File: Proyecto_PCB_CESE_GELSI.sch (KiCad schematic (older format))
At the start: 20 parts, among them IC1 SC2272L4, IC2 ASM1117-33, IC3 SN74LVC1G125DCKR, IC4 H5V3G

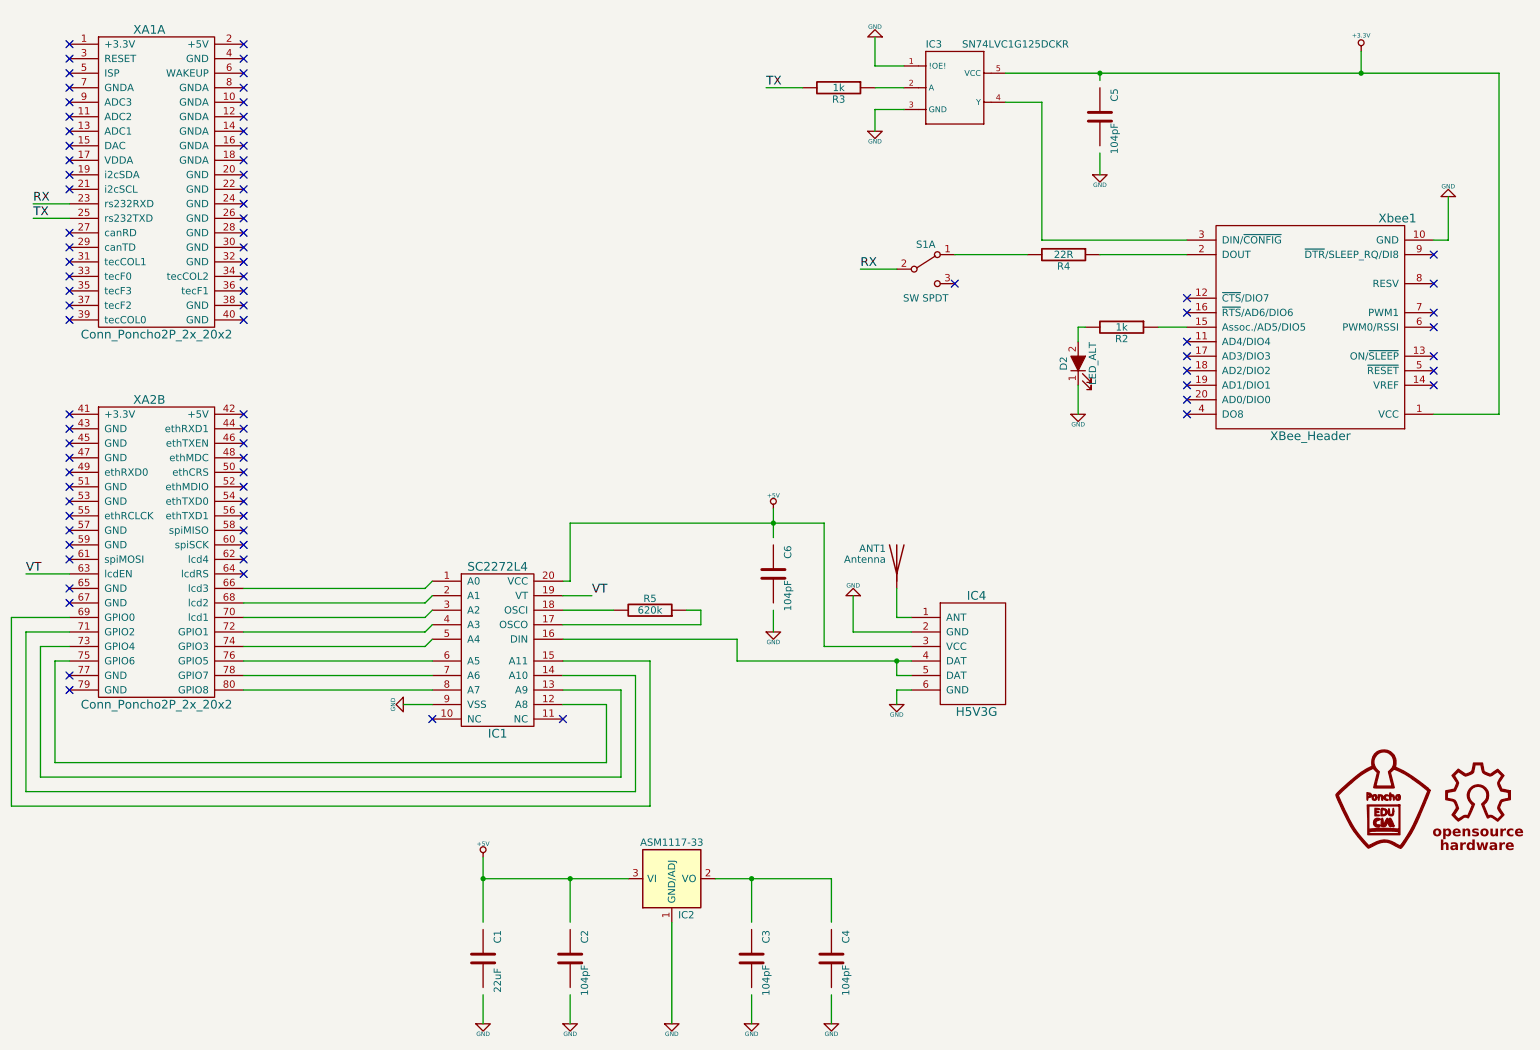
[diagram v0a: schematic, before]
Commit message: Avance hacia cierre de esquemático y comienzo de pcb
Falta sólo realizar comentarios con etiquetas en el esquemático, de los subsistemas. Y por otro lado ya se comenzó con el pcb, se avanzó para poder preguntar en clases dudas respecto al tema de ruteado.
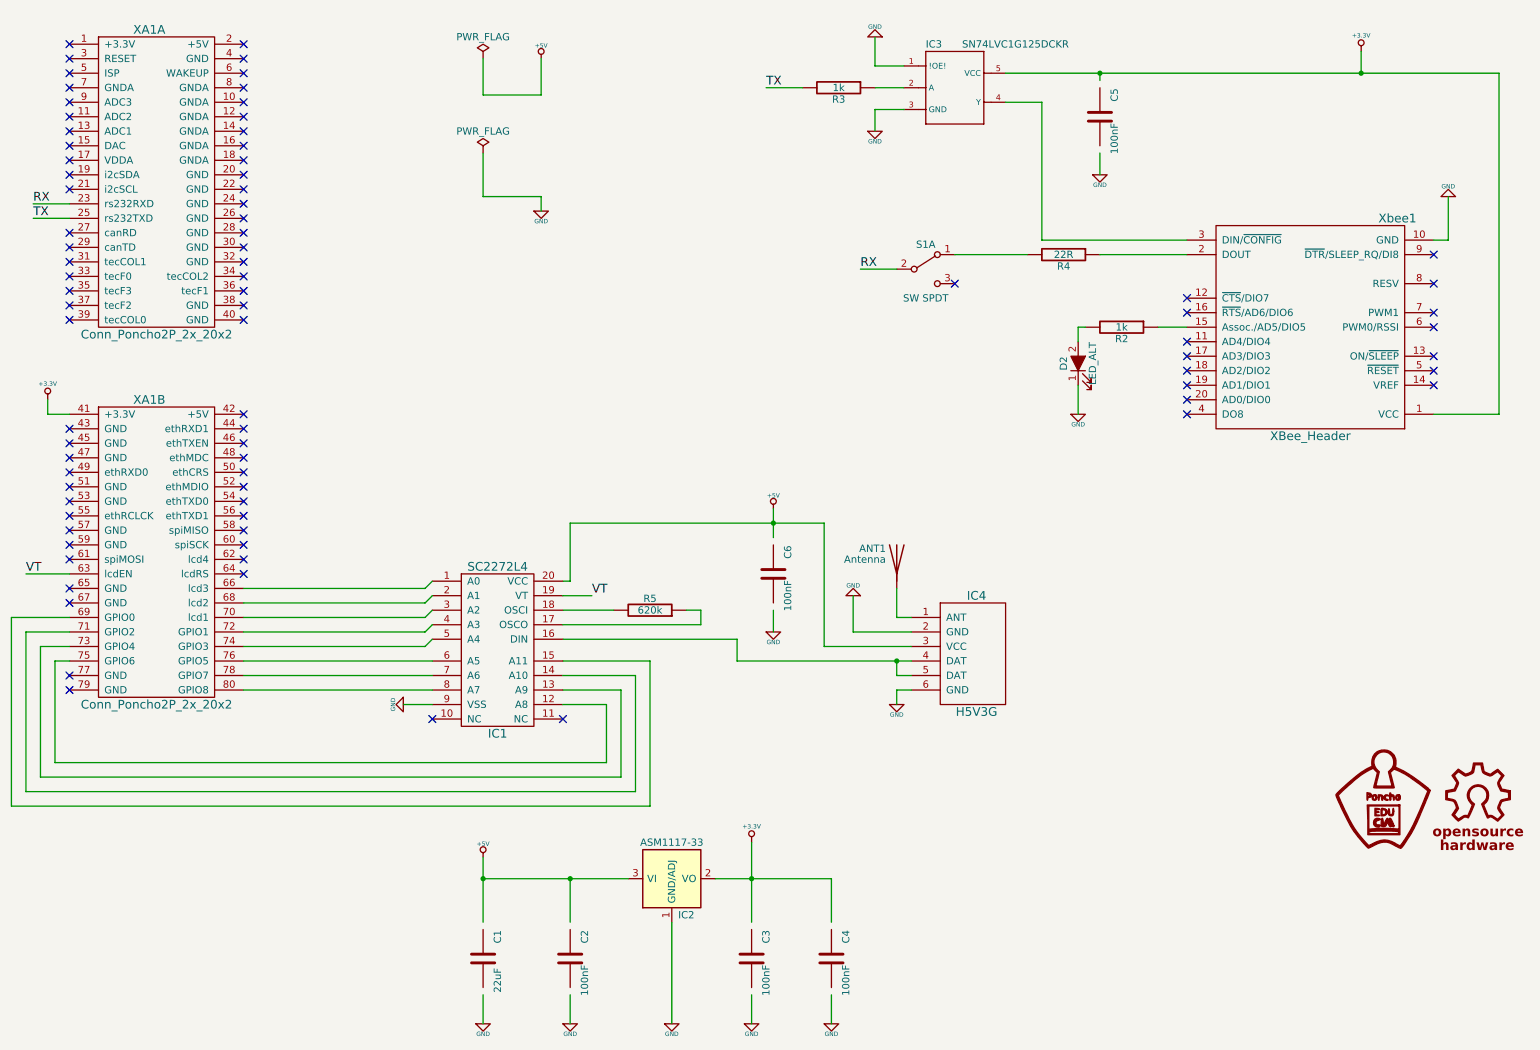
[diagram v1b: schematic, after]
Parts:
- ANT1: footprint (none) -> projectHuellas:antena
- C1: footprint (none) -> projectHuellas:C_0603_HandSoldering
- C2, C3, C4, C5, C6: value 104pF -> 100nF; footprint (none) -> projectHuellas:C_0603_HandSoldering
- D2: footprint (none) -> projectHuellas:D_0805
- IC1: footprint (none) -> projectHuellas:SSOP-20_5.3x7.2mm_Pitch0.65mm
- IC2: footprint TO_SOT_Packages_SMD:SOT-223 -> projectHuellas:SOT-223
- IC3: footprint SC-70-5 -> projectHuellas:SC-70-5
- IC4: footprint (none) -> projectHuellas:H5V3G
- R2, R3, R4, R5: footprint (none) -> projectHuellas:R_1206_HandSoldering
- S1: footprint (none) -> projectHuellas:SW_SPDT
- XA1: renamed from XA2; footprint (none) -> projectHuellas:Conn_Poncho_Completo
- XA1: footprint (none) -> projectHuellas:Conn_Poncho_Completo
- Xbee1: footprint (none) -> projectHuellas:XBEE-HEADER
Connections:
- wire segments 95 -> 103
- no-connect marks 83 -> 82

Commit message: Update en el proyecto
Se consolidaron datos en la mayoría de los componentes, como fabricante, parte dentro del fabricante, digikey, y descripción
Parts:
- C1: Desc (none) -> CAP CER 22UF 6.3V X5R 0603; Digikey# (none) -> 490-7611-1-ND; Manf (none) -> Murata Electronics North America; Manf# (none) -> GRM188R60J226MEA0D; Price (none) -> 0.24
- C2, C3, C4, C5, C6: Desc (none) -> CAP CER 0.1UF 6.3V X5R 0201; Digikey# (none) -> 478-5266-1-ND; Manf (none) -> AVX Corporation; Manf# (none) -> 02016D104KAT2A; Price (none) -> 0.10
- D2: Desc (none) -> LED GREEN DIFFUSED 0805 SMD; Digikey# (none) -> 475-1410-1-ND; Manf (none) -> OSRAM Opto Semiconductors Inc.; Manf# (none) -> LG R971-KN-1; Price (none) -> 0.25
- IC2: Desc (none) -> IC REG LDO 5V 1A SOT223; Digikey# (none) -> NCP1117ST50T3GOSCT-ND; Manf (none) -> ON Semiconductor; Manf# (none) -> NCP1117ST50T3G; Price (none) -> 0.50
- IC3: Desc (none) -> Buffer, Non-Inverting Element 1 Bit per Element Push-Pull O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; Description Buffer/Line%20Driver%201-CH%20Non-Inverting%203-ST%20CMOS%2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 -> (none); Digikey# (none) -> 296-11604-1-ND; Manf (none) -> Texas Instruments; Manf# (none) -> SN74LVC1G125DCKR; Price 0.14 USD -> 0.36 USD
- R2, R3: Desc (none) -> RES SMD 1K OHM 1% 1/4W 1206; Digikey# (none) -> 311-1.00KFRCT-ND; Manf (none) -> Yageo; Manf# (none) -> RC1206FR-071KL; Price (none) -> 0.10
- R4: Desc (none) -> RES SMD 22 OHM 5% 1/4W 1206; Digikey# (none) -> 311-22ERCT-ND; Manf (none) -> Yageo; Manf# (none) -> RC1206JR-0722RL; Price (none) -> 0.10
- R5: Desc (none) -> RES SMD 620K OHM 1% 1/4W 1206; Digikey# (none) -> 311-620KFRCT-ND; Manf (none) -> Yageo; Manf# (none) -> RC1206FR-07620KL; Price (none) -> 0.10
- S1: Desc (none) -> SWITCH SLIDE SPDT 300MA 4V; Digikey# (none) -> 679-1847-6-ND; Manf (none) -> APEM Inc.; Manf# (none) -> MA12RTR; Price (none) -> 0.93
- Xbee1: Desc (none) -> XBEE HEADER SOCKET 2MM 10PIN 2PK; Digikey# (none) -> 1528-1392-ND; Manf (none) -> Adafruit Industries LLC; Manf# (none) -> 366; Price (none) -> 0.95
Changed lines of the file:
@@
 F 2 "projectHuellas:SOT-223" H 5250 6200 50  0001 C CNN
 F 3 "" H 5350 6300 50  0001 C CNN
+F 4 "ON Semiconductor" H 5250 6550 60  0001 C CNN "Manf"
+F 5 "NCP1117ST50T3G" H 5250 6550 60  0001 C CNN "Manf#"
+F 6 "NCP1117ST50T3GOSCT-ND" H 5250 6550 60  0001 C CNN "Digikey#"
+F 7 "0.50" H 5250 6550 60  0001 C CNN "Price"
+F 8 "IC REG LDO 5V 1A SOT223" H 5250 6550 60  0001 C CNN "Desc"
 	1    5250 6550
 	1    0    0    -1
@@
 F 2 "projectHuellas:C_0603_HandSoldering" H 3950 7100 50  0001 C CNN
 F 3 "" H 3950 7100 50  0001 C CNN
+F 4 "Murata Electronics North America" H 3950 7100 60  0001 C CNN "Manf"
+F 5 "GRM188R60J226MEA0D" H 3950 7100 60  0001 C CNN "Manf#"
+F 6 "490-7611-1-ND" H 3950 7100 60  0001 C CNN "Digikey#"
+F 7 "0.24" V 3950 7100 60  0001 C CNN "Price"
+F 8 "CAP CER 22UF 6.3V X5R 0603" V 3950 7100 60  0001 C CNN "Desc"
 	1    3950 7100
 	1    0    0    -1
@@
 F 2 "projectHuellas:C_0603_HandSoldering" H 4550 7100 50  0001 C CNN
 F 3 "" H 4550 7100 50  0001 C CNN
+F 4 "AVX Corporation" H 4550 7100 60  0001 C CNN "Manf"
+F 5 "02016D104KAT2A" H 4550 7100 60  0001 C CNN "Manf#"
+F 6 "478-5266-1-ND" H 4550 7100 60  0001 C CNN "Digikey#"
+F 7 "0.10" V 4550 7100 60  0001 C CNN "Price"
+F 8 "CAP CER 0.1UF 6.3V X5R 0201" V 4550 7100 60  0001 C CNN "Desc"
 	1    4550 7100
 	1    0    0    -1
@@
 F 2 "projectHuellas:C_0603_HandSoldering" H 5800 7100 50  0001 C CNN
 F 3 "" H 5800 7100 50  0001 C CNN
+F 4 "AVX Corporation" H 5800 7100 60  0001 C CNN "Manf"
+F 5 "02016D104KAT2A" H 5800 7100 60  0001 C CNN "Manf#"
+F 6 "478-5266-1-ND" H 5800 7100 60  0001 C CNN "Digikey#"
+F 7 "0.10" V 5800 7100 60  0001 C CNN "Price"
+F 8 "CAP CER 0.1UF 6.3V X5R 0201" V 5800 7100 60  0001 C CNN "Desc"
 	1    5800 7100
 	1    0    0    -1
@@
 F 2 "projectHuellas:C_0603_HandSoldering" H 6350 7100 50  0001 C CNN
 F 3 "" H 6350 7100 50  0001 C CNN
+F 4 "AVX Corporation" H 6350 7100 60  0001 C CNN "Manf"
+F 5 "02016D104KAT2A" H 6350 7100 60  0001 C CNN "Manf#"
+F 6 "478-5266-1-ND" H 6350 7100 60  0001 C CNN "Digikey#"
+F 7 "0.10" V 6350 7100 60  0001 C CNN "Price"
+F 8 "CAP CER 0.1UF 6.3V X5R 0201" V 6350 7100 60  0001 C CNN "Desc"
 	1    6350 7100
 	1    0    0    -1
@@
 F 2 "projectHuellas:C_0603_HandSoldering" H 5950 4450 50  0001 C CNN
 F 3 "" H 5950 4450 50  0001 C CNN
+F 4 "AVX Corporation" H 5950 4450 60  0001 C CNN "Manf"
+F 5 "02016D104KAT2A" H 5950 4450 60  0001 C CNN "Manf#"
+F 6 "478-5266-1-ND" H 5950 4450 60  0001 C CNN "Digikey#"
+F 7 "0.10" V 5950 4450 60  0001 C CNN "Price"
+F 8 "CAP CER 0.1UF 6.3V X5R 0201" V 5950 4450 60  0001 C CNN "Desc"
 	1    5950 4450
 	1    0    0    -1
@@
 F 2 "projectHuellas:XBEE-HEADER" H 9400 2750 60  0001 C CNN
 F 3 "" H 9400 2750 60  0000 C CNN
+F 4 "Adafruit Industries LLC" H 9650 2750 60  0001 C CNN "Manf"
+F 5 "366" H 9650 2750 60  0001 C CNN "Manf#"
+F 6 "1528-1392-ND" H 9650 2750 60  0001 C CNN "Digikey#"
+F 7 "0.95" H 9650 2750 60  0001 C CNN "Price"
+F 8 "XBEE HEADER SOCKET 2MM 10PIN 2PK" H 9650 2750 60  0001 C CNN "Desc"
 	1    9650 2750
 	-1   0    0    1
@@
 F 2 "projectHuellas:SC-70-5" H 7200 1100 50  0001 L CNN
 F 3 "Texas Instruments" H 7200 1100 50  0001 L CNN
-F 4 "0.14 USD" H 7200 1100 50  0001 L CNN "Price"
-F 5 "Good" H 7200 1100 50  0001 L CNN "Availability"
-F 6 "SOP-5 Texas Instruments" H 7200 1100 50  0001 L CNN "Package"
-F 7 "SN74LVC1G125DCKR" H 7200 1100 50  0001 L CNN "MP"
-F 8 "Buffer/Line%20Driver%201-CH%20Non-Inverting%203-ST%20CMOS%205-Pin%20SC-70%20T/R" H 7200 1100 50  0001 L CNN "Description"
+F 4 "Texas Instruments" H 7200 1100 60  0001 C CNN "Manf"
+F 5 "SN74LVC1G125DCKR" H 7200 1100 60  0001 C CNN "Manf#"
+F 6 "296-11604-1-ND" H 7200 1100 60  0001 C CNN "Digikey#"
+F 7 "0.36 USD" H 7200 1100 50  0001 L CNN "Price"
+F 8 "Good" H 7200 1100 50  0001 L CNN "Availability"
+F 9 "SOP-5 Texas Instruments" H 7200 1100 50  0001 L CNN "Package"
+F 10 "SN74LVC1G125DCKR" H 7200 1100 50  0001 L CNN "MP"
+F 11 "Buffer, Non-Inverting Element 1 Bit per Element Push-Pull Output SC-70-5" H 7200 1100 50  0001 L CNN "Desc"
 	1    7200 1100
 	1    0    0    -1
@@
 F 2 "projectHuellas:C_0603_HandSoldering" H 8200 1300 50  0001 C CNN
 F 3 "" H 8200 1300 50  0001 C CNN
+F 4 "AVX Corporation" H 8200 1300 60  0001 C CNN "Manf"
+F 5 "02016D104KAT2A" H 8200 1300 60  0001 C CNN "Manf#"
+F 6 "478-5266-1-ND" H 8200 1300 60  0001 C CNN "Digikey#"
+F 7 "0.10" V 8200 1300 60  0001 C CNN "Price"
+F 8 "CAP CER 0.1UF 6.3V X5R 0201" V 8200 1300 60  0001 C CNN "Desc"
 	1    8200 1300
 	1    0    0    -1
@@
 F 2 "projectHuellas:R_1206_HandSoldering" H 7950 2250 50  0001 C CNN
 F 3 "" H 7950 2250 50  0001 C CNN
+F 4 "Yageo" H 7950 2250 60  0001 C CNN "Manf"
+F 5 "RC1206JR-0722RL" H 7950 2250 60  0001 C CNN "Manf#"
+F 6 "311-22ERCT-ND" H 7950 2250 60  0001 C CNN "Digikey#"
+F 7 "0.10" V 7950 2250 60  0001 C CNN "Price"
+F 8 "RES SMD 22 OHM 5% 1/4W 1206" V 7950 2250 60  0001 C CNN "Desc"
 	1    7950 2250
 	0    1    1    0
@@
 F 2 "projectHuellas:SW_SPDT" H 7000 2350 50  0001 C CNN
 F 3 "" H 7000 2350 50  0001 C CNN
+F 4 "APEM Inc." H 7000 2350 60  0001 C CNN "Manf"
+F 5 "MA12RTR" H 7000 2350 60  0001 C CNN "Manf#"
+F 6 "679-1847-6-ND" H 7000 2350 60  0001 C CNN "Digikey#"
+F 7 "0.93" H 7000 2350 60  0001 C CNN "Price"
+F 8 "SWITCH SLIDE SPDT 300MA 4V" H 7000 2350 60  0001 C CNN "Desc"
 	1    7000 2350
 	1    0    0    -1
@@
 F 2 "projectHuellas:R_1206_HandSoldering" H 8350 2750 50  0001 C CNN
 F 3 "" H 8350 2750 50  0001 C CNN
+F 4 "Yageo" H 8350 2750 60  0001 C CNN "Manf"
+F 5 "RC1206FR-071KL" H 8350 2750 60  0001 C CNN "Manf#"
+F 6 "311-1.00KFRCT-ND" H 8350 2750 60  0001 C CNN "Digikey#"
+F 7 "0.10" V 8350 2750 60  0001 C CNN "Price"
+F 8 "RES SMD 1K OHM 1% 1/4W 1206" V 8350 2750 60  0001 C CNN "Desc"
 	1    8350 2750
 	0    1    1    0
@@
 F 2 "projectHuellas:D_0805" H 8050 3000 50  0001 C CNN
 F 3 "" H 8050 3000 50  0001 C CNN
+F 4 "OSRAM Opto Semiconductors Inc." H 8050 3000 60  0001 C CNN "Manf"
+F 5 "LG R971-KN-1" H 8050 3000 60  0001 C CNN "Manf#"
+F 6 "475-1410-1-ND" H 8050 3000 60  0001 C CNN "Digikey#"
+F 7 "0.25" H 8050 3000 60  0001 C CNN "Price"
+F 8 "LED GREEN DIFFUSED 0805 SMD" H 8050 3000 60  0001 C CNN "Desc"
 	1    8050 3000
 	0    -1   -1   0
@@
 F 2 "projectHuellas:R_1206_HandSoldering" H 6400 1100 50  0001 C CNN
 F 3 "" H 6400 1100 50  0001 C CNN
+F 4 "Yageo" H 6400 1100 60  0001 C CNN "Manf"
+F 5 "RC1206FR-071KL" H 6400 1100 60  0001 C CNN "Manf#"
+F 6 "311-1.00KFRCT-ND" H 6400 1100 60  0001 C CNN "Digikey#"
+F 7 "0.10" V 6400 1100 60  0001 C CNN "Price"
+F 8 "RES SMD 1K OHM 1% 1/4W 1206" V 6400 1100 60  0001 C CNN "Desc"
 	1    6400 1100
 	0    1    1    0
@@
 F 2 "projectHuellas:R_1206_HandSoldering" H 5100 4700 50  0001 C CNN
 F 3 "" H 5100 4700 50  0001 C CNN
+F 4 "Yageo" H 5100 4700 60  0001 C CNN "Manf"
+F 5 "RC1206FR-07620KL" H 5100 4700 60  0001 C CNN "Manf#"
+F 6 "311-620KFRCT-ND" H 5100 4700 60  0001 C CNN "Digikey#"
+F 7 "0.10" V 5100 4700 60  0001 C CNN "Price"
+F 8 "RES SMD 620K OHM 1% 1/4W 1206" V 5100 4700 60  0001 C CNN "Desc"
 	1    5100 4700
 	0    1    -1   0
